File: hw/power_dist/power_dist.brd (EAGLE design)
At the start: 80 x 50 mm, 69 parts, among them J1 JST-ZH6SMT_VERT, J2 JST-PH4SMT_VERT, J3 JST-PH5VERT, P1 XT30P, P2 XT30P, P3 XT30P, P4 XT30P, P5 XT30P, P6 XT30P, P7 XT90PW-M, Q1 PSMN4R8-100BSEJ, Q2 PSMN4R8-100BSEJ, Q3 PSMN4R8-100BSEJ, Q4 MF-DSC-SOT233-BSS138, Q5 MF-DSC-SOT233-MMBT3906, Q6 MF-DSC-SOT233-MMBT3904, U1 MAX15062AATA+T, U2 STM32G474CEU6, U3 LM5066IPMHE/NOPB, U4 TCAN334G

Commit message: power_dist r4: Assign part numbers
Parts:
- R4: value 47k 1% -> 140k 1%
- R5: value 15k 1% -> 40.2k 1%
- R6: value 47k 1% -> 100k 1%
- R7: value 19.1k 1% -> 40.2k 1%

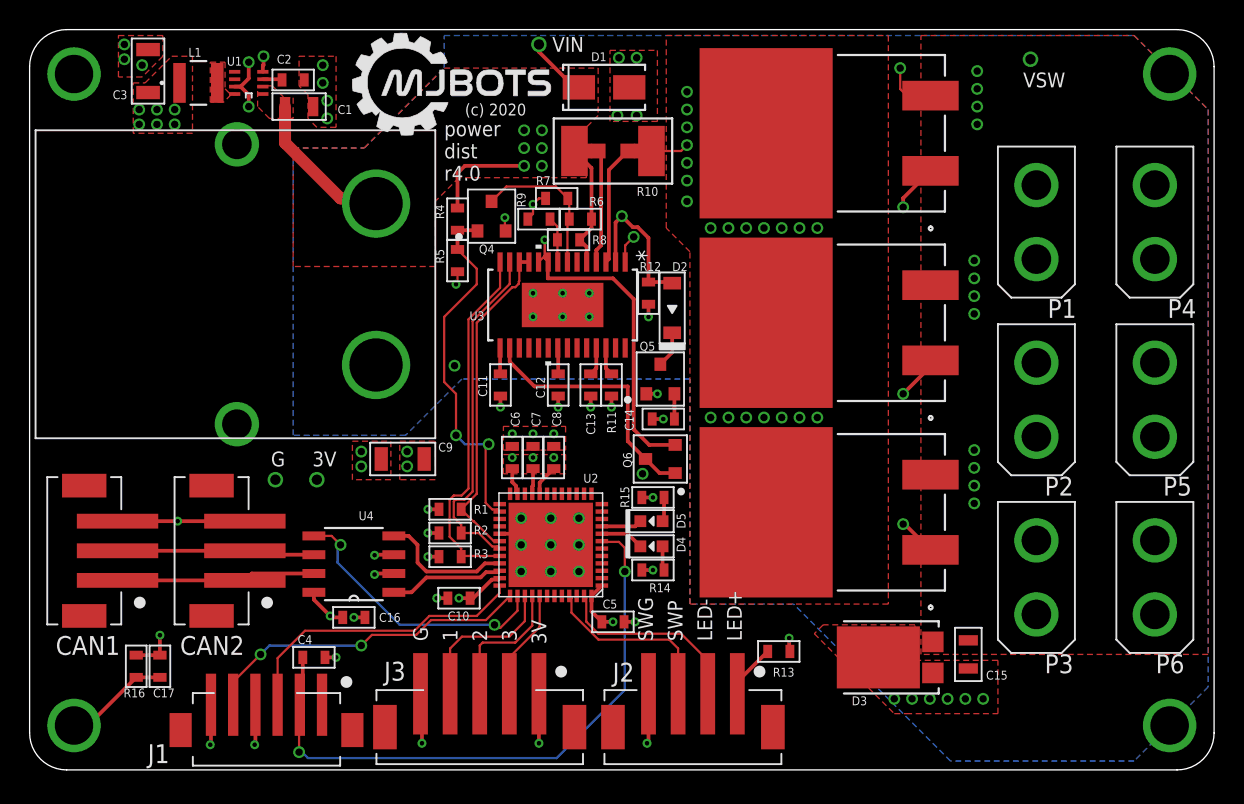
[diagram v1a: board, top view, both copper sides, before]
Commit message: power_dist r4: Update XT90 silk to be closer to actual part
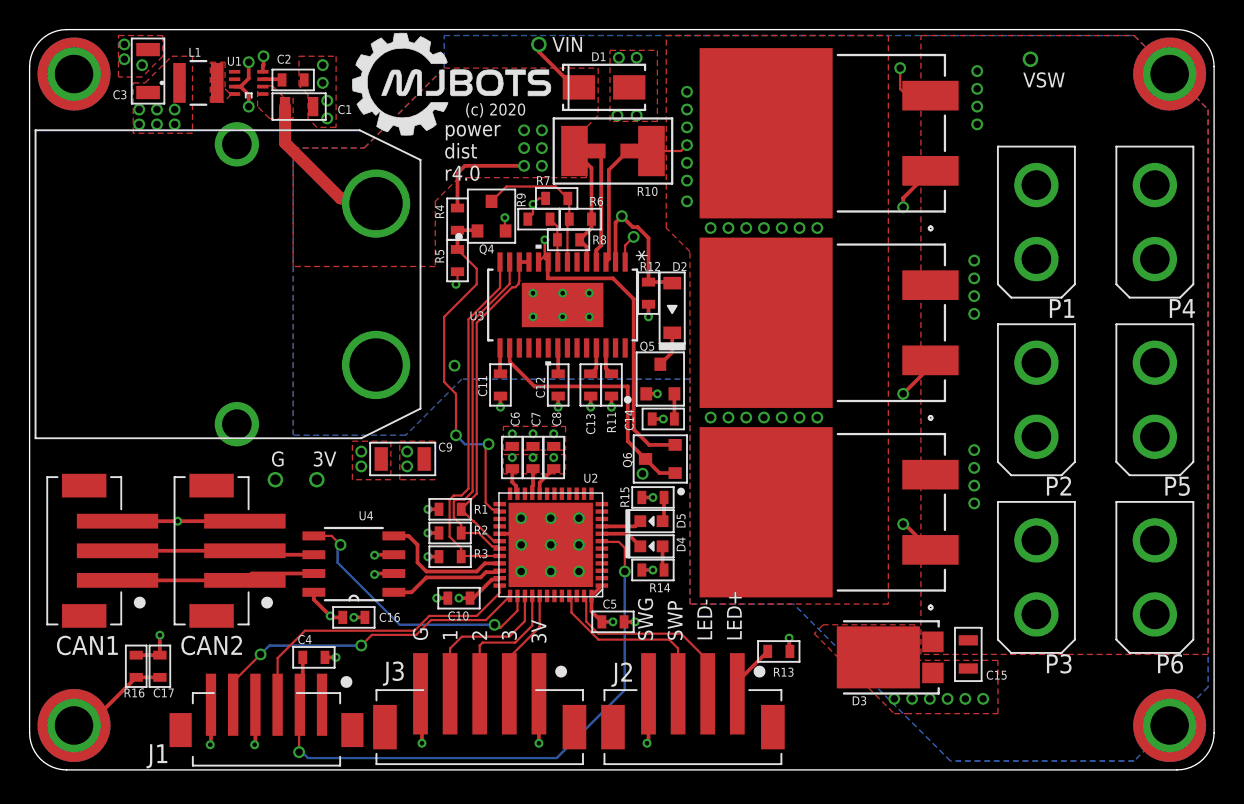
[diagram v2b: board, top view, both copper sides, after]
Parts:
- P7: device precharge:XT90PW-M -> power_dist:XT90PW-M
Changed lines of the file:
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@@
 <attribute name="POPULATE" value="0" x="117.64" y="-19.86" size="1.778" layer="27" display="off"/>
 </element>
-<element name="P7" library="precharge" package="XT90PW-M" value="XT90PW-M" x="23.4" y="32.8" smashed="yes" rot="R90">
+<element name="P7" library="power_dist" package="XT90PW-M" value="XT90PW-M" x="23.4" y="32.8" smashed="yes" rot="R90">
 <attribute name="POPULATE" value="0" x="23.4" y="32.8" size="1.778" layer="27" rot="R90" display="off"/>
 </element>
